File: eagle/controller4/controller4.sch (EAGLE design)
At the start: 62 parts, among them J4 USB-MICROB, J7 2X6 FEMALE, Q3 check_pins, X1 1501_04

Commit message: controller4 progress
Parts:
- removed HIGHSIDESWITCH: MOSFET-PCHANNELNDP6020P_20V_24A_LOW_VGS_TH, SparkFun-DiscreteSemi:MOSFET-PCHANNELNDP6020P_20V_24A_LOW_VGS_TH
- added Q2: FDD4141TO252, transistor-fet:FDD4141TO252
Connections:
- net BATT_VCC: now also Q2.S; no longer HIGHSIDESWITCH.S
- net CAM_OUT: now also Q2.D; no longer HIGHSIDESWITCH.D
- net N$36: now also Q2.G; no longer HIGHSIDESWITCH.G
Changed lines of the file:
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@@
 <grid distance="0.1" unitdist="inch" unit="inch" style="lines" multiple="1" display="no" altdistance="0.01" altunitdist="inch" altunit="inch"/>
 <layers>
-<layer number="1" name="Top" color="4" fill="1" visible="yes" active="no"/>
-<layer number="16" name="Bottom" color="1" fill="1" visible="yes" active="no"/>
-<layer number="17" name="Pads" color="2" fill="1" visible="yes" active="no"/>
-<layer number="18" name="Vias" color="2" fill="1" visible="yes" active="no"/>
-<layer number="19" name="Unrouted" color="6" fill="1" visible="yes" active="no"/>
-<layer number="20" name="Dimension" color="15" fill="1" visible="yes" active="no"/>
-<layer number="21" name="tPlace" color="7" fill="1" visible="yes" active="no"/>
-<layer number="22" name="bPlace" color="7" fill="1" visible="yes" active="no"/>
-<layer number="23" name="tOrigins" color="15" fill="1" visible="yes" active="no"/>
-<layer number="24" name="bOrigins" color="15" fill="1" visible="yes" active="no"/>
-<layer number="25" name="tNames" color="7" fill="1" visible="yes" active="no"/>
-<layer number="26" name="bNames" color="7" fill="1" visible="yes" active="no"/>
-<layer number="27" name="tValues" color="7" fill="1" visible="yes" active="no"/>
-<layer number="28" name="bValues" color="7" fill="1" visible="yes" active="no"/>
+<layer number="1" name="Top" color="4" fill="1" visible="no" active="no"/>
+<layer number="16" name="Bottom" color="1" fill="1" visible="no" active="no"/>
+<layer number="17" name="Pads" color="2" fill="1" visible="no" active="no"/>
+<layer number="18" name="Vias" color="2" fill="1" visible="no" active="no"/>
+<layer number="19" name="Unrouted" color="6" fill="1" visible="no" active="no"/>
+<layer number="20" name="Dimension" color="15" fill="1" visible="no" active="no"/>
+<layer number="21" name="tPlace" color="7" fill="1" visible="no" active="no"/>
+<layer number="22" name="bPlace" color="7" fill="1" visible="no" active="no"/>
+<layer number="23" name="tOrigins" color="15" fill="1" visible="no" active="no"/>
+<layer number="24" name="bOrigins" color="15" fill="1" visible="no" active="no"/>
+<layer number="25" name="tNames" color="7" fill="1" visible="no" active="no"/>
+<layer number="26" name="bNames" color="7" fill="1" visible="no" active="no"/>
+<layer number="27" name="tValues" color="7" fill="1" visible="no" active="no"/>
+<layer number="28" name="bValues" color="7" fill="1" visible="no" active="no"/>
 <layer number="29" name="tStop" color="7" fill="3" visible="no" active="no"/>
 <layer number="30" name="bStop" color="7" fill="6" visible="no" active="no"/>
@@
 <layer number="35" name="tGlue" color="7" fill="4" visible="no" active="no"/>
 <layer number="36" name="bGlue" color="7" fill="5" visible="no" active="no"/>
-<layer number="37" name="tTest" color="7" fill="1" visible="yes" active="no"/>
-<layer number="38" name="bTest" color="7" fill="1" visible="yes" active="no"/>
+<layer number="37" name="tTest" color="7" fill="1" visible="no" active="no"/>
+<layer number="38" name="bTest" color="7" fill="1" visible="no" active="no"/>
 <layer number="39" name="tKeepout" color="4" fill="11" visible="no" active="no"/>
 <layer number="40" name="bKeepout" color="1" fill="11" visible="no" active="no"/>
@@
 <layer number="44" name="Drills" color="7" fill="1" visible="no" active="no"/>
 <layer number="45" name="Holes" color="7" fill="1" visible="no" active="no"/>
-<layer number="46" name="Milling" color="3" fill="1" visible="yes" active="no"/>
-<layer number="47" name="Measures" color="7" fill="1" visible="yes" active="no"/>
-<layer number="48" name="Document" color="7" fill="1" visible="yes" active="no"/>
-<layer number="49" name="Reference" color="7" fill="1" visible="yes" active="no"/>
-<layer number="50" name="dxf" color="7" fill="1" visible="yes" active="no"/>
-<layer number="51" name="tDocu" color="7" fill="1" visible="yes" active="no"/>
-<layer number="52" name="bDocu" color="7" fill="1" visible="yes" active="no"/>
-<layer number="53" name="tGND_GNDA" color="7" fill="9" visible="yes" active="no"/>
-<layer number="54" name="bGND_GNDA" color="1" fill="9" visible="yes" active="no"/>
-<layer number="56" name="wert" color="7" fill="1" visible="yes" active="no"/>
-<layer number="57" name="tCAD" color="7" fill="1" visible="yes" active="no"/>
-<layer number="59" name="tCarbon" color="7" fill="1" visible="yes" active="no"/>
-<layer number="60" name="bCarbon" color="7" fill="1" visible="yes" active="no"/>
+<layer number="46" name="Milling" color="3" fill="1" visible="no" active="no"/>
+<layer number="47" name="Measures" color="7" fill="1" visible="no" active="no"/>
+<layer number="48" name="Document" color="7" fill="1" visible="no" active="no"/>
+<layer number="49" name="Reference" color="7" fill="1" visible="no" active="no"/>
+<layer number="50" name="dxf" color="7" fill="1" visible="no" active="no"/>
+<layer number="51" name="tDocu" color="7" fill="1" visible="no" active="no"/>
+<layer number="52" name="bDocu" color="7" fill="1" visible="no" active="no"/>
+<layer number="53" name="tGND_GNDA" color="7" fill="9" visible="no" active="no"/>
+<layer number="54" name="bGND_GNDA" color="1" fill="9" visible="no" active="no"/>
+<layer number="56" name="wert" color="7" fill="1" visible="no" active="no"/>
+<layer number="57" name="tCAD" color="7" fill="1" visible="no" active="no"/>
+<layer number="59" name="tCarbon" color="7" fill="1" visible="no" active="no"/>
+<layer number="60" name="bCarbon" color="7" fill="1" visible="no" active="no"/>
 <layer number="90" name="Modules" color="5" fill="1" visible="yes" active="yes"/>
 <layer number="91" name="Nets" color="2" fill="1" visible="yes" active="yes"/>
@@
 <part name="RB3" library="SparkFun-Resistors" deviceset="RESISTOR" device="1206" value="10k"/>
 <part name="SUPPLY22" library="SparkFun-Aesthetics" deviceset="VCC" device=""/>
-<part name="HIGHSIDESWITCH" library="SparkFun-DiscreteSemi" deviceset="MOSFET-PCHANNEL" device="NDP6020P_20V_24A_LOW_VGS_TH" value=""/>
 <part name="T_HSS" library="SparkFun-DiscreteSemi" deviceset="TRANSISTOR_NPN" device="2N3904"/>
 <part name="R17" library="SparkFun-Resistors" deviceset="RESISTOR" device="1206" value="1k"/>
@@
 <part name="J3" library="SparkFun-Connectors" deviceset="M02" device="LOCK_LONGPADS"/>
 <part name="S1" library="SparkFun-Electromechanical" deviceset="SWITCH-SPDT" device="PTH_LOCK"/>
+<part name="Q2" library="transistor-fet" deviceset="FDD4141" device="TO252"/>
 </parts>
 <sheets>
@@
 <instance part="RB3" gate="G$1" x="180.34" y="195.58"/>
 <instance part="SUPPLY22" gate="G$1" x="185.42" y="195.58" rot="R270"/>
-<instance part="HIGHSIDESWITCH" gate="G$1" x="424.18" y="38.1" smashed="yes">
-<attribute name="NAME" x="431.8" y="27.94" size="1.778" layer="95" rot="R90"/>
-<attribute name="VALUE" x="429.26" y="38.1" size="1.778" layer="96"/>
-</instance>
 <instance part="T_HSS" gate="G$1" x="403.86" y="48.26" rot="R180"/>
 <instance part="R17" gate="G$1" x="401.32" y="30.48" rot="R90"/>
@@
 <instance part="J3" gate="G$1" x="66.04" y="40.64" rot="R90"/>
 <instance part="S1" gate="1" x="99.06" y="226.06" rot="R270"/>
+<instance part="Q2" gate="G$1" x="426.72" y="35.56" rot="R180"/>
 </instances>
 <busses>
@@
 </segment>
 <segment>
-<pinref part="HIGHSIDESWITCH" gate="G$1" pin="D"/>
-<label x="424.18" y="53.34" size="1.778" layer="95" rot="R90"/>
-<wire x1="424.18" y1="43.18" x2="424.18" y2="53.34" width="0.1524" layer="91"/>
+<pinref part="Q2" gate="G$1" pin="D"/>
+<wire x1="424.18" y1="40.64" x2="424.18" y2="63.5" width="0.1524" layer="91"/>
+<label x="424.18" y="63.5" size="1.778" layer="95"/>
 </segment>
 </net>
@@
 </segment>
 <segment>
-<pinref part="HIGHSIDESWITCH" gate="G$1" pin="S"/>
-<wire x1="424.18" y1="33.02" x2="424.18" y2="25.4" width="0.1524" layer="91"/>
 <label x="424.18" y="12.7" size="1.778" layer="95" rot="R90"/>
 <pinref part="R17" gate="G$1" pin="1"/>
 <wire x1="424.18" y1="25.4" x2="424.18" y2="12.7" width="0.1524" layer="91"/>
 <wire x1="401.32" y1="25.4" x2="424.18" y2="25.4" width="0.1524" layer="91"/>
+<pinref part="Q2" gate="G$1" pin="S"/>
+<wire x1="424.18" y1="25.4" x2="424.18" y2="30.48" width="0.1524" layer="91"/>
 <junction x="424.18" y="25.4"/>
 </segment>
@@
 <wire x1="401.32" y1="38.1" x2="401.32" y2="35.56" width="0.1524" layer="91"/>
 <pinref part="T_HSS" gate="G$1" pin="C"/>
-<pinref part="HIGHSIDESWITCH" gate="G$1" pin="G"/>
 <wire x1="416.56" y1="38.1" x2="401.32" y2="38.1" width="0.1524" layer="91"/>
 <wire x1="401.32" y1="38.1" x2="401.32" y2="43.18" width="0.1524" layer="91"/>
 <junction x="401.32" y="38.1"/>
-</segment>
-</net>
+<pinref part="Q2" gate="G$1" pin="G"/>
+<wire x1="429.26" y1="33.02" x2="431.8" y2="33.02" width="0.1524" layer="91"/>
+<wire x1="431.8" y1="33.02" x2="431.8" y2="45.72" width="0.1524" layer="91"/>
+<wire x1="431.8" y1="45.72" x2="416.56" y2="45.72" width="0.1524" layer="91"/>
+<wire x1="416.56" y1="45.72" x2="416.56" y2="38.1" width="0.1524" layer="91"/>
+</segment>
+</net>

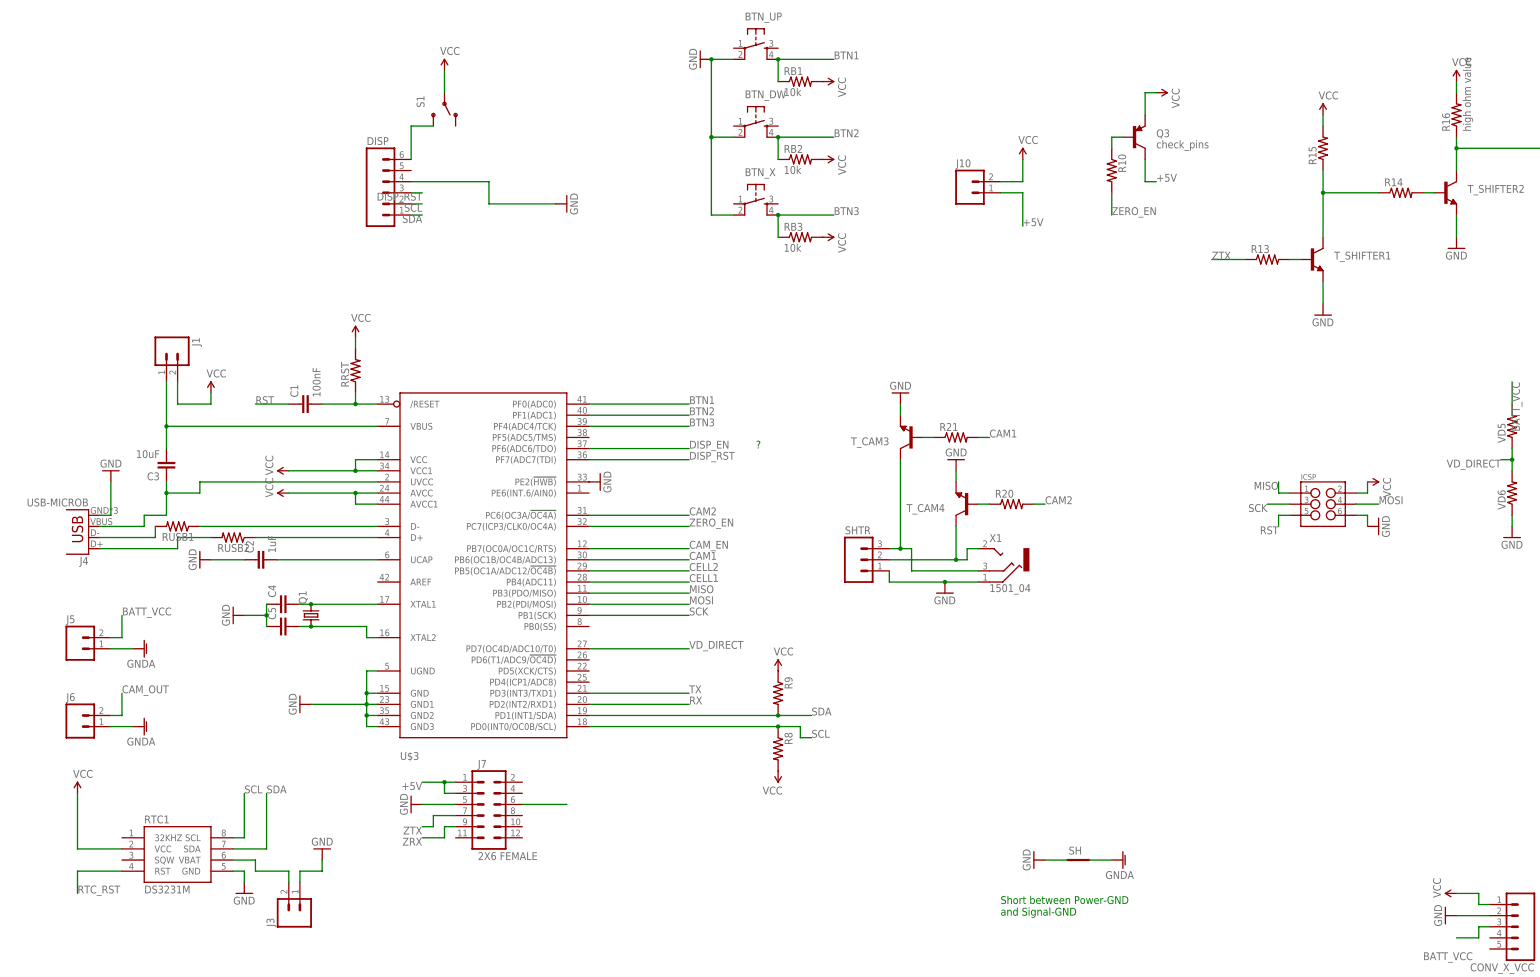
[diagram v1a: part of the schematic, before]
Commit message: controller4: added switch (battery -> USB)
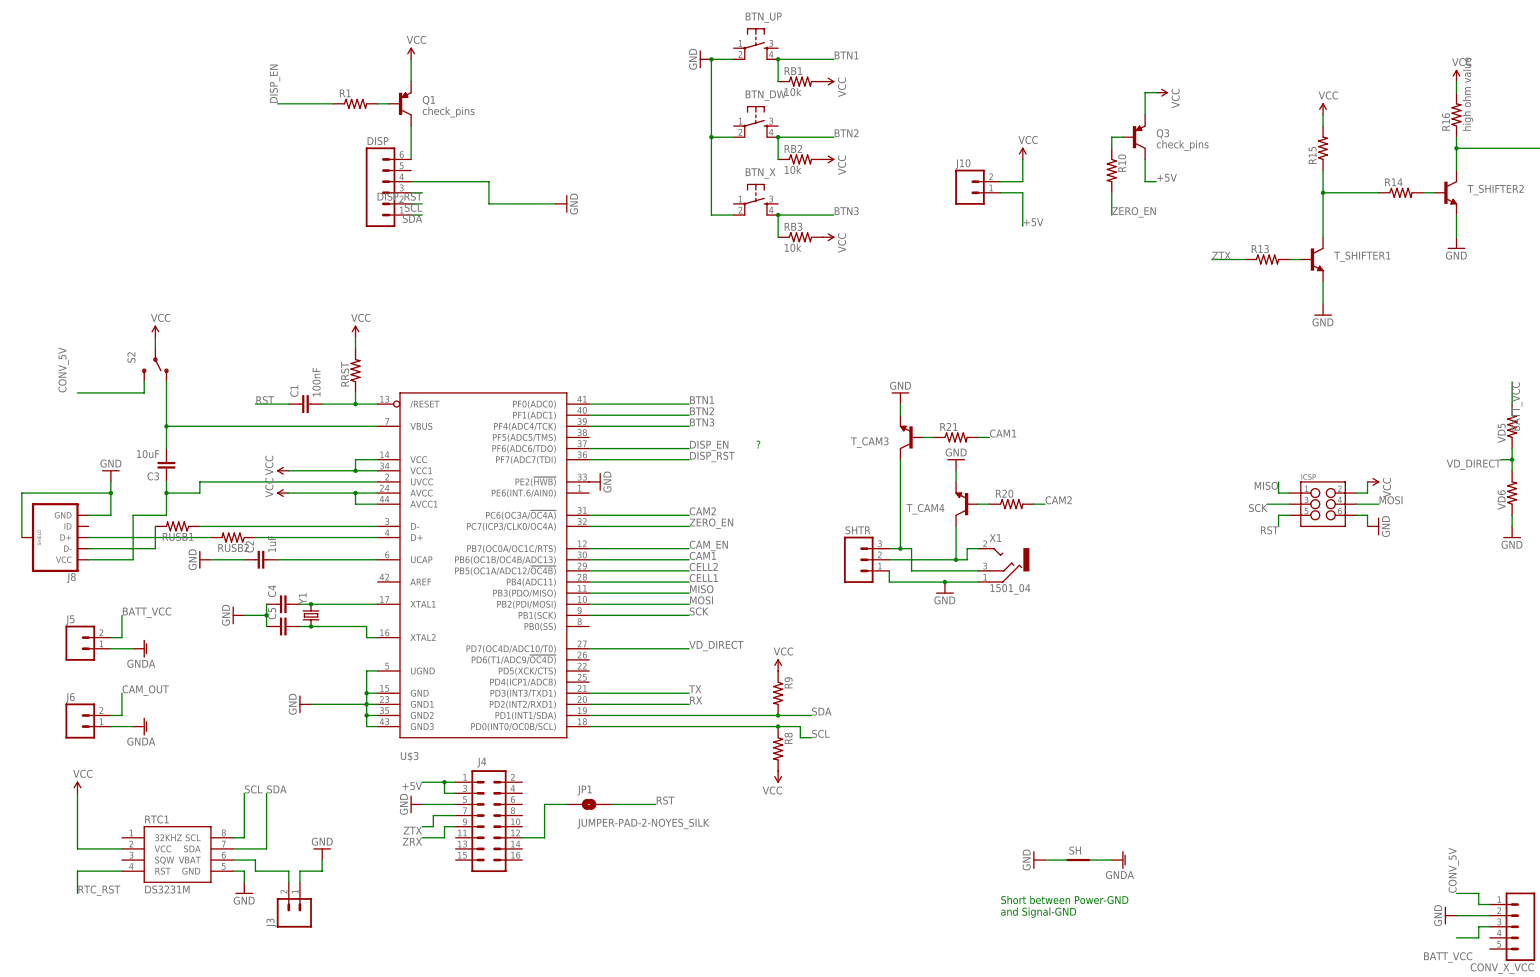
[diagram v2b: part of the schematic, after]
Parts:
- removed J1: (no value), SparkFun-Connectors:M02LOCK
- removed J7: 2X6 FEMALE, SparkFun-Connectors:M06X2PTH_FEMALE
- removed S1: (no value), SparkFun-Electromechanical:SWITCH-SPDTPTH_LOCK
- added J8: (no value), SparkFun-Connectors:USB_MICROB_PLUGCONN-11752
- added JP1: JUMPER-PAD-2-NOYES_SILK, SparkFun-Passives:JUMPER-PAD-2-NOYES_SILK
- added R1: (no value), SparkFun-Resistors:RESISTOR1206
- added S2: (no value), SparkFun-Electromechanical:SWITCH-SPDTPTH_LOCK
- added Y1: (no value), SparkFun-FreqCtrl:CRYSTALHC49US
- J4: value USB-MICROB -> (none); device SparkFun-Connectors:USB-MICROB -> SparkFun-Connectors:M08X2
- Q1: value (none) -> check_pins; device adafruit:CRYSTALMM20SS -> SparkFun-DiscreteSemi:TRANSISTOR_PNPTO92
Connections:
- removed net N$16: J7.6
- new net CONV_5V: CONV_X_VCC.1, S2.S
- new net N$12: Q1.B, R1.2
- new net N$7: J4.12, JP1.1
- net +5V: now also J4.1, J4.3; no longer J7.1, J7.3
- net DISP_EN: now also R1.1
- net GND: now also J4.5, J8.GND, J8.SHIELD; no longer J4.GND, J7.5
- net N$10: now also S2.O; no longer J1.1
- net N$11: now also J8.D-; no longer J4.D-
- net N$14: now also J8.D+; no longer J4.D+
- net N$22: now also J8.VCC; no longer J4.VBUS
- net N$6: now also Q1.C; no longer S1.S
- net N$8: now also Y1.2; no longer Q1.2
- net N$9: now also Y1.1; no longer Q1.1
- net RST: now also JP1.2
- net VCC: now also S2.P; no longer CONV_X_VCC.1, J1.2, S1.P
- net ZRX: now also J4.9; no longer J7.9
- net ZTX: now also J4.7; no longer J7.7
